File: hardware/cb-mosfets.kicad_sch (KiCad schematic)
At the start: 30 parts

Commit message: fixes
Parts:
- removed C913, C914, C915, C916, C917: 100n, Capacitor_SMD:C_0805_2012Metric, symbol Device:C_Small
- removed R907, R908, R909, R910, R911, R912, R913, R914, R915, R916, R917: 100, Resistor_SMD:R_1206_3216Metric, symbol Device:R_Small
- added C902, C903, C904, C905, C906, C907: C_Small, symbol Device:C_Small
- added R901: R_Small, symbol Device:R_Small
- C901, C908, C909, C910, C911, C912: value 100n -> C_Small; footprint Capacitor_SMD:C_0805_2012Metric -> (none)
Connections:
- net CELL10: now also R901.1
- net GND: now also C902.2
- net VC0: now also C902.1
- net VC1: now also C903.2
- net VC10: now also C912.1, R901.2; no longer C908.1
- net VC2: now also C903.1, C904.2, C905.2
- net VC3: now also C904.1, C905.1, C906.2
- net VC4: now also C906.1, C907.2
- net VC5: now also C908.2, C907.1; no longer C912.2
- net VC6: now also C908.1, C909.2; no longer C911.2, C912.1
- net VC7: now also C909.1; no longer C911.1
- net VC8: now also C911.2; no longer C909.2
- net VC9: now also C911.1, C912.2; no longer C908.2, C909.1
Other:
- sheet cb_mosfet renamed cb_mosfet_0
- added sheet cb_mosfet_1 (cb_mosfet.kicad_sch)
- added sheet cb_mosfet_10 (cb_mosfet.kicad_sch)
- added sheet cb_mosfet_2 (cb_mosfet.kicad_sch)
- added sheet cb_mosfet_3 (cb_mosfet.kicad_sch)
- added sheet cb_mosfet_4 (cb_mosfet.kicad_sch)
- added sheet cb_mosfet_5 (cb_mosfet.kicad_sch)
- added sheet cb_mosfet_6 (cb_mosfet.kicad_sch)
- added sheet cb_mosfet_7 (cb_mosfet.kicad_sch)
- added sheet cb_mosfet_8 (cb_mosfet.kicad_sch)
- added sheet cb_mosfet_9 (cb_mosfet.kicad_sch)
- sheet cb_mosfet_0 ports: added cell_bottom, cell_top, vc_bottom; removed none
- moved on the sheet: JP901, JP902, JP903, JP904, JP905, JP907, JP909

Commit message: cleanup
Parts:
- C901, C902, C903, C904, C905, C906, C907, C908, C909, C910, C911, C912: value C_Small -> 100n 50V 0805; LCSC (none) -> C49678
- R901: value R_Small -> 100R 0805; LCSC (none) -> C17408

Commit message: add bat{en adc}
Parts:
- added Q901, Q902: Q_NMOS_GDS, symbol Transistor_FET:Q_NMOS_GDS
- added R902, R903, R904, R905: 100R 0805, symbol Device:R_Small
- renumbered C902 to C901, C904 to C902, C906 to C903, C908 to C904, C910 to C905, C912 to C906, C903 to C907, C901 to C908, C905 to C909, C907 to C910, C909 to C911, C911 to C912, JP909 to JP901, JP901 to JP902, JP902 to JP903, JP907 to JP904, JP904 to JP906, JP903 to JP907, JP906 to JP908
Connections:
- net CELL10: now also Q901.3 (S), R904.1
- net GND: now also Q902.3 (S), R903.2
- new net: Q901.1 (G), R904.2, R905.1
- new net: Q901.2 (D), R902.1
- new net: Q902.2 (D), R905.2
- new net BAT.ADC: R902.2, R903.1
- new net BAT.EN: Q902.1 (G)
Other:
- moved on the sheet: C901, C902, C903, C904, C905, C906, C907, C908, C909, C910, C911, C912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

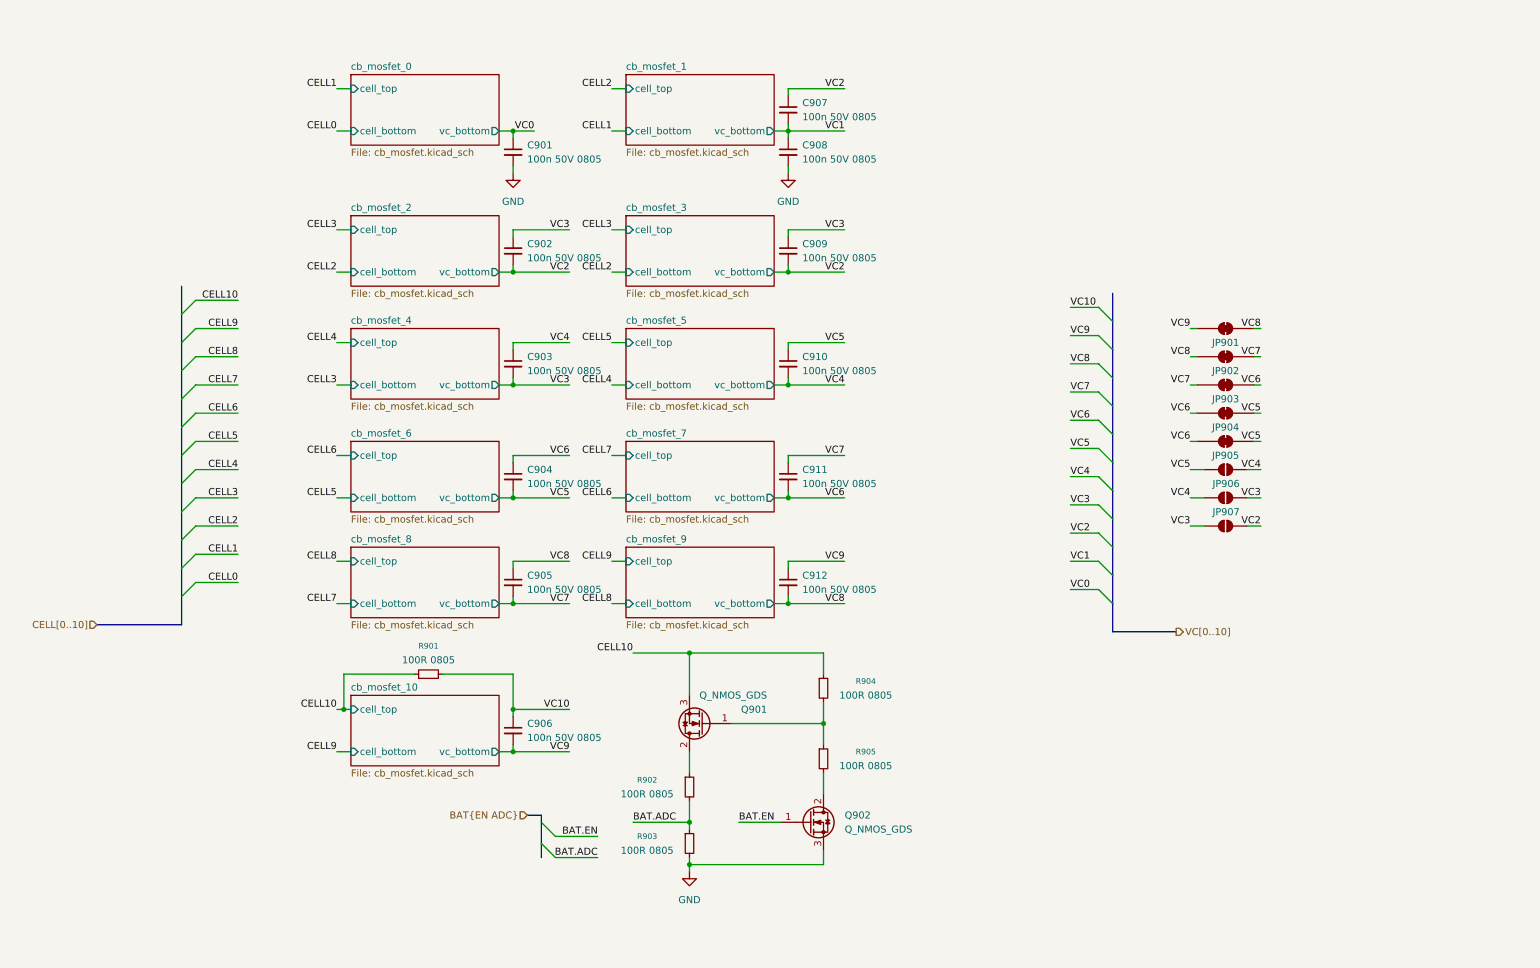
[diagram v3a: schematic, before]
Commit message: simplify page
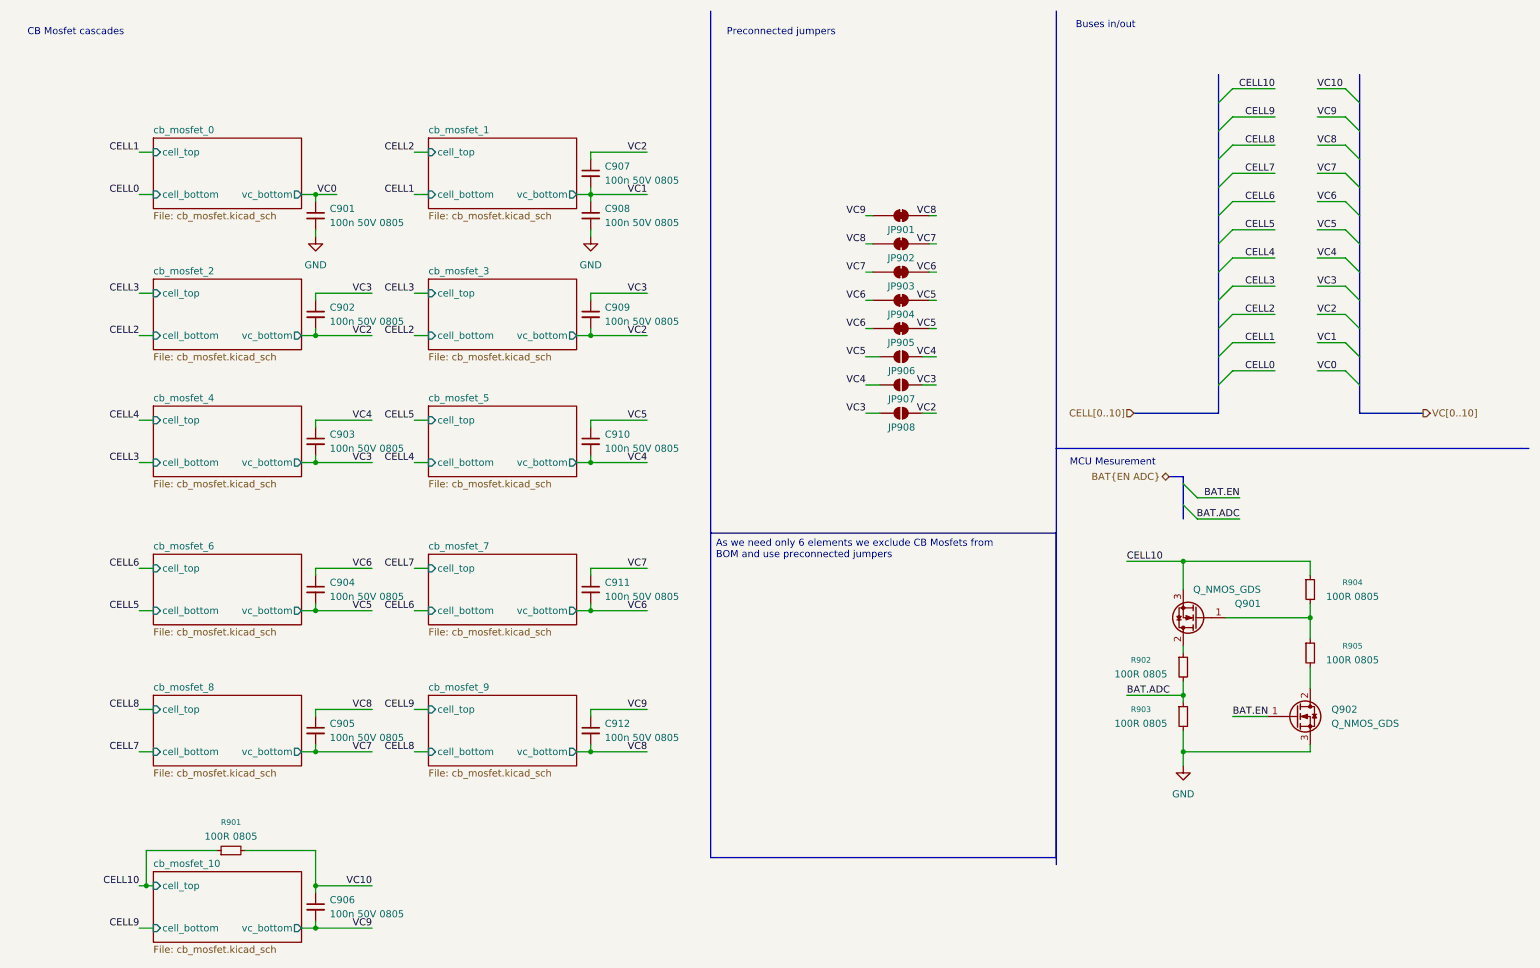
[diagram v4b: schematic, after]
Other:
- note added: "Buses in/out"
- note added: "CB Mosfet cascades"
- note added: "MCU Mesurement"
- note added: "Preconnected jumpers"
- moved on the sheet: C901, C902, C903, C904, C905, C906, C907, C908, C909, C910, C911, C912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
